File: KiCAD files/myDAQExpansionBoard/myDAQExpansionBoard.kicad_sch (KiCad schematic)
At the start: 71 parts, among them J1 Conn_01x05_Male, J2 Conn_01x05_Male, J3 Conn_01x08_Male, J4 OSTV7XX3151, J5 Screw_Terminal_01x02, J6 Screw_Terminal_01x02, J7 Screw_Terminal_01x01, J8 Screw_Terminal_01x01, SW1 SW_SPDT, SW2 SW_SPDT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

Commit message: update
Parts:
- R1, R20: value 1k -> 4k7
- R10, R11, R13, R14, R15, R16, R8: value 680 -> 4k7
- R5: value 1k -> 2k
- R7: value 1k -> 619
- R9: value 1k -> 6k8
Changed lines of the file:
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@@
     (in_bom yes) (on_board yes)
     (property "Reference" "R7" (id 0) (at 177.419 45.974 90))
-    (property "Value" "1k" (id 1) (at 177.419 48.514 90))
+    (property "Value" "619" (id 1) (at 177.419 48.514 90))
     (property "Footprint" "Resistor_SMD:R_0603_1608Metric" (id 2) (at 177.419 50.292 90)
       (effects (font (size 1.27 1.27)) hide)
@@
     (in_bom yes) (on_board yes)
     (property "Reference" "R9" (id 0) (at 177.419 58.674 90))
-    (property "Value" "1k" (id 1) (at 177.419 61.214 90))
+    (property "Value" "6k8" (id 1) (at 177.419 61.214 90))
     (property "Footprint" "Resistor_SMD:R_0603_1608Metric" (id 2) (at 177.419 62.992 90)
       (effects (font (size 1.27 1.27)) hide)
@@
     (in_bom yes) (on_board yes)
     (property "Reference" "R8" (id 0) (at 166.751 70.104 90))
-    (property "Value" "680" (id 1) (at 166.751 72.009 90))
+    (property "Value" "4k7" (id 1) (at 166.751 72.009 90))
     (property "Footprint" "Resistor_SMD:R_0603_1608Metric" (id 2) (at 166.751 73.787 90)
       (effects (font (size 1.27 1.27)) hide)
@@
     (in_bom yes) (on_board yes)
     (property "Reference" "R1" (id 0) (at 177.419 16.764 90))
-    (property "Value" "1k" (id 1) (at 177.419 19.304 90))
+    (property "Value" "4k7" (id 1) (at 177.419 19.304 90))
     (property "Footprint" "Resistor_SMD:R_0603_1608Metric" (id 2) (at 177.419 21.082 90)
       (effects (font (size 1.27 1.27)) hide)
@@
     (in_bom yes) (on_board yes)
     (property "Reference" "R10" (id 0) (at 166.751 74.549 90))
-    (property "Value" "680" (id 1) (at 166.751 76.454 90))
+    (property "Value" "4k7" (id 1) (at 166.751 76.454 90))
     (property "Footprint" "Resistor_SMD:R_0603_1608Metric" (id 2) (at 166.751 78.232 90)
       (effects (font (size 1.27 1.27)) hide)
@@
     (in_bom yes) (on_board yes)
     (property "Reference" "R11" (id 0) (at 166.751 78.994 90))
-    (property "Value" "680" (id 1) (at 166.751 80.899 90))
+    (property "Value" "4k7" (id 1) (at 166.751 80.899 90))
     (property "Footprint" "Resistor_SMD:R_0603_1608Metric" (id 2) (at 166.751 82.677 90)
       (effects (font (size 1.27 1.27)) hide)
@@
     (in_bom yes) (on_board yes)
     (property "Reference" "R16" (id 0) (at 166.751 96.774 90))
-    (property "Value" "680" (id 1) (at 166.751 98.679 90))
+    (property "Value" "4k7" (id 1) (at 166.751 98.679 90))
     (property "Footprint" "Resistor_SMD:R_0603_1608Metric" (id 2) (at 166.751 100.457 90)
       (effects (font (size 1.27 1.27)) hide)
@@
     (in_bom yes) (on_board yes)
     (property "Reference" "R13" (id 0) (at 166.751 83.439 90))
-    (property "Value" "680" (id 1) (at 166.751 85.344 90))
+    (property "Value" "4k7" (id 1) (at 166.751 85.344 90))
     (property "Footprint" "Resistor_SMD:R_0603_1608Metric" (id 2) (at 166.751 87.122 90)
       (effects (font (size 1.27 1.27)) hide)
@@
     (in_bom yes) (on_board yes)
     (property "Reference" "R5" (id 0) (at 177.419 32.639 90))
-    (property "Value" "1k" (id 1) (at 177.419 35.179 90))
+    (property "Value" "2k" (id 1) (at 177.419 35.179 90))
     (property "Footprint" "Resistor_SMD:R_0603_1608Metric" (id 2) (at 177.419 36.957 90)
       (effects (font (size 1.27 1.27)) hide)
@@
     (in_bom yes) (on_board yes)
     (property "Reference" "R20" (id 0) (at 216.535 90.297 0))
-    (property "Value" "1k" (id 1) (at 219.71 90.297 90))
+    (property "Value" "4k7" (id 1) (at 219.71 90.297 90))
     (property "Footprint" "Resistor_SMD:R_0603_1608Metric" (id 2) (at 217.932 90.297 90)
       (effects (font (size 1.27 1.27)) hide)
@@
     (in_bom yes) (on_board yes)
     (property "Reference" "R15" (id 0) (at 166.751 92.329 90))
-    (property "Value" "680" (id 1) (at 166.751 94.234 90))
+    (property "Value" "4k7" (id 1) (at 166.751 94.234 90))
     (property "Footprint" "Resistor_SMD:R_0603_1608Metric" (id 2) (at 166.751 96.012 90)
       (effects (font (size 1.27 1.27)) hide)
@@
     (in_bom yes) (on_board yes)
     (property "Reference" "R14" (id 0) (at 166.751 87.884 90))
-    (property "Value" "680" (id 1) (at 166.751 89.789 90))
+    (property "Value" "4k7" (id 1) (at 166.751 89.789 90))
     (property "Footprint" "Resistor_SMD:R_0603_1608Metric" (id 2) (at 166.751 91.567 90)
       (effects (font (size 1.27 1.27)) hide)
@@
     )
     (path "/433b0c6c-361b-44cd-99c3-351dd671e9c9"
-      (reference "R1") (unit 1) (value "1k") (footprint "Resistor_SMD:R_0603_1608Metric")
+      (reference "R1") (unit 1) (value "4k7") (footprint "Resistor_SMD:R_0603_1608Metric")
     )
     (path "/f78db9fb-cb90-4b5a-a4c3-fa1ddcd96b2f"
@@
     )
     (path "/bc772a1b-5451-41db-9c2f-d7edb0c376e2"
-      (reference "R5") (unit 1) (value "1k") (footprint "Resistor_SMD:R_0603_1608Metric")
+      (reference "R5") (unit 1) (value "2k") (footprint "Resistor_SMD:R_0603_1608Metric")
     )
     (path "/ca6ccc26-d3b9-4b88-bfa0-85358f769c5a"
@@
     )
     (path "/085dede5-e78e-4e86-8f9f-0e5465cc00b9"
-      (reference "R7") (unit 1) (value "1k") (footprint "Resistor_SMD:R_0603_1608Metric")
+      (reference "R7") (unit 1) (value "619") (footprint "Resistor_SMD:R_0603_1608Metric")
     )
     (path "/2ba9d9c0-5d0a-4be1-afe4-2de9cfa25c42"
-      (reference "R8") (unit 1) (value "680") (footprint "Resistor_SMD:R_0603_1608Metric")
+      (reference "R8") (unit 1) (value "4k7") (footprint "Resistor_SMD:R_0603_1608Metric")
     )
     (path "/15ef9b16-b6d9-46b2-bd55-e3bd55127ab3"
-      (reference "R9") (unit 1) (value "1k") (footprint "Resistor_SMD:R_0603_1608Metric")
+      (reference "R9") (unit 1) (value "6k8") (footprint "Resistor_SMD:R_0603_1608Metric")
     )
     (path "/525c708d-edd2-4368-bbec-bf4b6e9c0ace"
-      (reference "R10") (unit 1) (value "680") (footprint "Resistor_SMD:R_0603_1608Metric")
+      (reference "R10") (unit 1) (value "4k7") (footprint "Resistor_SMD:R_0603_1608Metric")
     )
     (path "/7212c595-395e-40b8-bda9-f190b9683d3b"
-      (reference "R11") (unit 1) (value "680") (footprint "Resistor_SMD:R_0603_1608Metric")
+      (reference "R11") (unit 1) (value "4k7") (footprint "Resistor_SMD:R_0603_1608Metric")
     )
     (path "/b4dfd47d-e445-4115-b914-f93c8ca70c01"
@@
     )
     (path "/b4ebc770-9ee9-4695-b41e-2c705582fd44"
-      (reference "R13") (unit 1) (value "680") (footprint "Resistor_SMD:R_0603_1608Metric")
+      (reference "R13") (unit 1) (value "4k7") (footprint "Resistor_SMD:R_0603_1608Metric")
     )
     (path "/fd4b6262-dad5-45ce-9480-0b0623b0e919"
-      (reference "R14") (unit 1) (value "680") (footprint "Resistor_SMD:R_0603_1608Metric")
+      (reference "R14") (unit 1) (value "4k7") (footprint "Resistor_SMD:R_0603_1608Metric")
     )
     (path "/ed2f2cb4-07ba-406b-bf66-2ddd22ebe99b"
-      (reference "R15") (unit 1) (value "680") (footprint "Resistor_SMD:R_0603_1608Metric")
+      (reference "R15") (unit 1) (value "4k7") (footprint "Resistor_SMD:R_0603_1608Metric")
     )
     (path "/ab9b29b0-c429-48b0-9aad-ff945e1e65b3"
-      (reference "R16") (unit 1) (value "680") (footprint "Resistor_SMD:R_0603_1608Metric")
+      (reference "R16") (unit 1) (value "4k7") (footprint "Resistor_SMD:R_0603_1608Metric")
     )
     (path "/97abf834-da84-49dd-ace7-84d78a8c1b0f"
@@
     )
     (path "/d27373d0-8f97-432f-9664-fb2c66cf74ea"
-      (reference "R20") (unit 1) (value "1k") (footprint "Resistor_SMD:R_0603_1608Metric")
+      (reference "R20") (unit 1) (value "4k7") (footprint "Resistor_SMD:R_0603_1608Metric")
     )
     (path "/951d8e55-0983-48e1-a0c4-bac48479355a"

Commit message: update
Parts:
- R10, R11, R13, R14, R15, R16, R8: value 4k7 -> 2k
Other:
- note added: "*2k otpronici za crveni 7segm display (4.6V VCC)"
- note removed: "SN74LS74 (6kn u electronic centru)"
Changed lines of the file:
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@@
     (effects (font (size 2 2)) (justify left bottom))
   )
-  (text "SN74LS74 (6kn u electronic centru)" (at 97.282 104.14 0)
+  (text "*2k otpronici za crveni 7segm display (4.6V VCC)" (at 97.282 104.14 0)
     (effects (font (size 1.27 1.27)) (justify left bottom))
   )
@@
     (in_bom yes) (on_board yes)
     (property "Reference" "R8" (id 0) (at 166.751 70.104 90))
-    (property "Value" "4k7" (id 1) (at 166.751 72.009 90))
+    (property "Value" "2k" (id 1) (at 166.751 72.009 90))
     (property "Footprint" "Resistor_SMD:R_0603_1608Metric" (id 2) (at 166.751 73.787 90)
       (effects (font (size 1.27 1.27)) hide)
@@
     (in_bom yes) (on_board yes)
     (property "Reference" "R10" (id 0) (at 166.751 74.549 90))
-    (property "Value" "4k7" (id 1) (at 166.751 76.454 90))
+    (property "Value" "2k" (id 1) (at 166.751 76.454 90))
     (property "Footprint" "Resistor_SMD:R_0603_1608Metric" (id 2) (at 166.751 78.232 90)
       (effects (font (size 1.27 1.27)) hide)
@@
     (in_bom yes) (on_board yes)
     (property "Reference" "R11" (id 0) (at 166.751 78.994 90))
-    (property "Value" "4k7" (id 1) (at 166.751 80.899 90))
+    (property "Value" "2k" (id 1) (at 166.751 80.899 90))
     (property "Footprint" "Resistor_SMD:R_0603_1608Metric" (id 2) (at 166.751 82.677 90)
       (effects (font (size 1.27 1.27)) hide)
@@
     (in_bom yes) (on_board yes)
     (property "Reference" "R16" (id 0) (at 166.751 96.774 90))
-    (property "Value" "4k7" (id 1) (at 166.751 98.679 90))
+    (property "Value" "2k" (id 1) (at 166.751 98.679 90))
     (property "Footprint" "Resistor_SMD:R_0603_1608Metric" (id 2) (at 166.751 100.457 90)
       (effects (font (size 1.27 1.27)) hide)
@@
     (in_bom yes) (on_board yes)
     (property "Reference" "R13" (id 0) (at 166.751 83.439 90))
-    (property "Value" "4k7" (id 1) (at 166.751 85.344 90))
+    (property "Value" "2k" (id 1) (at 166.751 85.344 90))
     (property "Footprint" "Resistor_SMD:R_0603_1608Metric" (id 2) (at 166.751 87.122 90)
       (effects (font (size 1.27 1.27)) hide)
@@
     (in_bom yes) (on_board yes)
     (property "Reference" "R15" (id 0) (at 166.751 92.329 90))
-    (property "Value" "4k7" (id 1) (at 166.751 94.234 90))
+    (property "Value" "2k" (id 1) (at 166.751 94.234 90))
     (property "Footprint" "Resistor_SMD:R_0603_1608Metric" (id 2) (at 166.751 96.012 90)
       (effects (font (size 1.27 1.27)) hide)
@@
     (in_bom yes) (on_board yes)
     (property "Reference" "R14" (id 0) (at 166.751 87.884 90))
-    (property "Value" "4k7" (id 1) (at 166.751 89.789 90))
+    (property "Value" "2k" (id 1) (at 166.751 89.789 90))
     (property "Footprint" "Resistor_SMD:R_0603_1608Metric" (id 2) (at 166.751 91.567 90)
       (effects (font (size 1.27 1.27)) hide)
@@
     )
     (path "/2ba9d9c0-5d0a-4be1-afe4-2de9cfa25c42"
-      (reference "R8") (unit 1) (value "4k7") (footprint "Resistor_SMD:R_0603_1608Metric")
+      (reference "R8") (unit 1) (value "2k") (footprint "Resistor_SMD:R_0603_1608Metric")
     )
     (path "/15ef9b16-b6d9-46b2-bd55-e3bd55127ab3"
@@
     )
     (path "/525c708d-edd2-4368-bbec-bf4b6e9c0ace"
-      (reference "R10") (unit 1) (value "4k7") (footprint "Resistor_SMD:R_0603_1608Metric")
+      (reference "R10") (unit 1) (value "2k") (footprint "Resistor_SMD:R_0603_1608Metric")
     )
     (path "/7212c595-395e-40b8-bda9-f190b9683d3b"
-      (reference "R11") (unit 1) (value "4k7") (footprint "Resistor_SMD:R_0603_1608Metric")
+      (reference "R11") (unit 1) (value "2k") (footprint "Resistor_SMD:R_0603_1608Metric")
     )
     (path "/b4dfd47d-e445-4115-b914-f93c8ca70c01"
@@
     )
     (path "/b4ebc770-9ee9-4695-b41e-2c705582fd44"
-      (reference "R13") (unit 1) (value "4k7") (footprint "Resistor_SMD:R_0603_1608Metric")
+      (reference "R13") (unit 1) (value "2k") (footprint "Resistor_SMD:R_0603_1608Metric")
     )
     (path "/fd4b6262-dad5-45ce-9480-0b0623b0e919"
-      (reference "R14") (unit 1) (value "4k7") (footprint "Resistor_SMD:R_0603_1608Metric")
+      (reference "R14") (unit 1) (value "2k") (footprint "Resistor_SMD:R_0603_1608Metric")
     )
     (path "/ed2f2cb4-07ba-406b-bf66-2ddd22ebe99b"
-      (reference "R15") (unit 1) (value "4k7") (footprint "Resistor_SMD:R_0603_1608Metric")
+      (reference "R15") (unit 1) (value "2k") (footprint "Resistor_SMD:R_0603_1608Metric")
     )
     (path "/ab9b29b0-c429-48b0-9aad-ff945e1e65b3"
-      (reference "R16") (unit 1) (value "4k7") (footprint "Resistor_SMD:R_0603_1608Metric")
+      (reference "R16") (unit 1) (value "2k") (footprint "Resistor_SMD:R_0603_1608Metric")
     )
     (path "/97abf834-da84-49dd-ace7-84d78a8c1b0f"

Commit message: Update myDAQExpansionBoard.kicad_sch
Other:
- note added: "*2k otpronici za crveni 7segm display"
- note added: "7SEGM + IC SN74LS47"
- note removed: "*2k otpronici za crveni 7segm display (4.6V VCC)"
- note removed: "7SEGM + IC SN74LS74"
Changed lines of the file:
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@@
     (effects (font (size 2 2)) (justify left bottom))
   )
-  (text "*2k otpronici za crveni 7segm display (4.6V VCC)" (at 97.282 104.14 0)
+  (text "*2k otpronici za crveni 7segm display" (at 90.17 108.585 0)
     (effects (font (size 1.27 1.27)) (justify left bottom))
   )
@@
     (effects (font (size 2 2)) (justify left bottom))
   )
-  (text "7SEGM + IC SN74LS74" (at 96.901 70.739 0)
+  (text "7SEGM + IC SN74LS47" (at 96.901 70.739 0)
     (effects (font (size 2 2)) (justify left bottom))
   )

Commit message: BOMv1
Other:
- note added: "BILJEŠKE: - BOM se nalazi u bom folderu, datoteka se zove myDAQExpansionBoard.xlsx"
- note removed: "MONTAŽA: - jumperi moraju biti oni koji imaju ručicu"
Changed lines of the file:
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@@
     (effects (font (size 2 2)) (justify left bottom))
   )
-  (text "MONTAŽA:\n- jumperi moraju biti oni koji imaju ručicu"
-    (at 15.24 161.29 0)
-    (effects (font (size 1.27 1.27)) (justify left bottom))
+  (text "BILJEŠKE:\n\n- BOM se nalazi u bom folderu, datoteka se zove myDAQExpansionBoard.xlsx"
+    (at 15.24 185.42 0)
+    (effects (font (size 2.54 2.54)) (justify left bottom))
   )
   (text "MON. RUPE" (at 14.986 88.9 0)

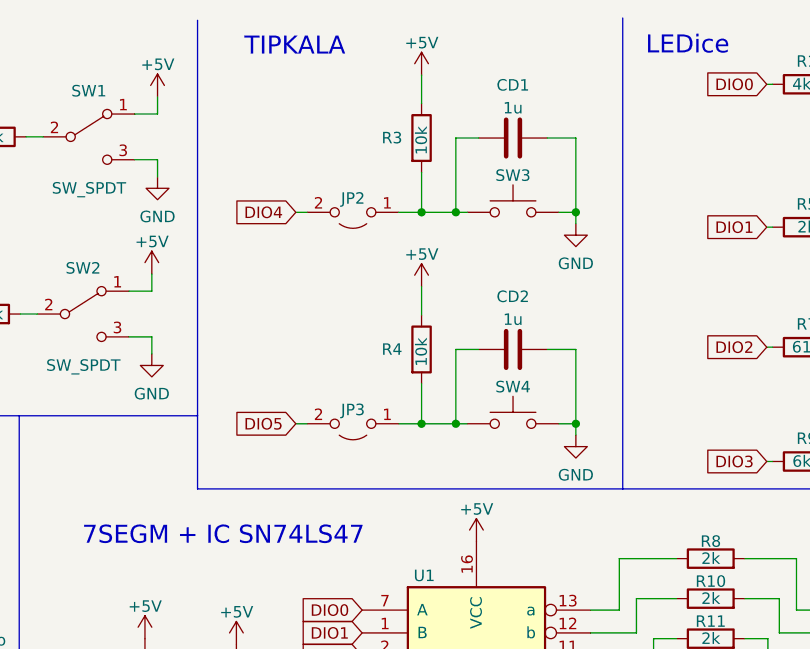
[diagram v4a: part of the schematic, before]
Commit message: Added resistor for RC circuit
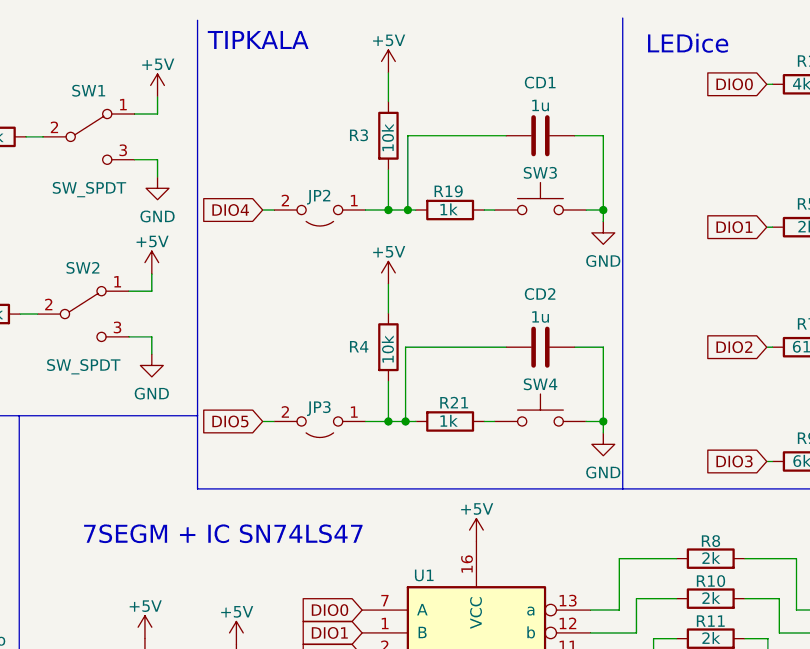
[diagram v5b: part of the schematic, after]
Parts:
- added R19, R21: 1k, Resistor_SMD:R_0603_1608Metric, symbol Device:R
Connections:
- net at CD1.1, JP2.1 (A), R3.2: now also R19.2; no longer SW3.1
- net at CD2.1, JP3.1 (A), R4.2: now also R21.2; no longer SW4.1
- new net: R21.1, SW4.1
- new net: R19.1, SW3.1
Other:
- moved on the sheet: CD1, CD2, JP2, JP3, R3, R4, SW3, SW4

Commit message: update
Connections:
- net DIO0: now also JP2.2 (B); no longer R1.1, U1.7 (A), U4.5 (IN1)
- net DIO1: now also R1.1, U1.7 (A); no longer R5.1, U1.1 (B)
- net DIO2: now also JP3.2 (B); no longer R7.1, U1.2 (C), U4.10 (IN3)
- net DIO3: now also R5.1, U1.1 (B), U4.5 (IN1); no longer R9.1, U1.6 (D), U4.12 (IN4)
- net DIO4: now also JP4.2 (B); no longer JP2.2 (B)
- net DIO5: now also R7.1, U1.2 (C), U4.10 (IN3); no longer JP3.2 (B)
- net DIO7: now also R9.1, U1.6 (D), U4.12 (IN4); no longer JP4.2 (B)

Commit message: v1rev2
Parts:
- SW1, SW2: footprint Library:we01014042 -> Library:500SSP1S1M2QEA
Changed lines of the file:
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@@
     (property "Reference" "SW1" (id 0) (at 97.663 20.066 0))
     (property "Value" "SW_SPDT" (id 1) (at 97.663 30.861 0))
-    (property "Footprint" "Library:we01014042" (id 2) (at 97.663 25.146 0)
+    (property "Footprint" "Library:500SSP1S1M2QEA" (id 2) (at 97.663 25.146 0)
       (effects (font (size 1.27 1.27)) hide)
     )
@@
     (property "Reference" "SW2" (id 0) (at 97.028 39.751 0))
     (property "Value" "SW_SPDT" (id 1) (at 97.028 50.546 0))
-    (property "Footprint" "Library:we01014042" (id 2) (at 97.028 44.831 0)
+    (property "Footprint" "Library:500SSP1S1M2QEA" (id 2) (at 97.028 44.831 0)
       (effects (font (size 1.27 1.27)) hide)
     )
@@
     )
     (path "/7078f9f8-f76c-4524-96a7-1f5a2c6a03e5"
-      (reference "SW1") (unit 1) (value "SW_SPDT") (footprint "Library:we01014042")
+      (reference "SW1") (unit 1) (value "SW_SPDT") (footprint "Library:500SSP1S1M2QEA")
     )
     (path "/bb50f314-d057-4b1a-9b4d-ff176329b7ae"
-      (reference "SW2") (unit 1) (value "SW_SPDT") (footprint "Library:we01014042")
+      (reference "SW2") (unit 1) (value "SW_SPDT") (footprint "Library:500SSP1S1M2QEA")
     )
     (path "/90f2d58e-a255-450d-bc74-dbc1a747cc3e"

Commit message: update
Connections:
- net DIO0: now also JP1.2 (B); no longer JP2.2 (B)
- net DIO2: now also JP4.2 (B); no longer JP3.2 (B)
- net DIO4: now also JP3.2 (B); no longer JP4.2 (B)
- net DIO6: now also JP2.2 (B); no longer JP1.2 (B)
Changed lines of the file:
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@@
     )
   )
-  (global_label "DIO4" (shape input) (at 67.818 44.831 180) (fields_autoplaced)
+  (global_label "DIO4" (shape input) (at 116.967 56.769 180) (fields_autoplaced)
     (effects (font (size 1.27 1.27)) (justify right))
-    (property "Intersheet References" "${INTERSHEET_REFS}" (id 0) (at 60.9901 44.7516 0)
+    (property "Intersheet References" "${INTERSHEET_REFS}" (id 0) (at 110.1391 56.6896 0)
       (effects (font (size 1.27 1.27)) (justify right) hide)
     )
@@
     )
   )
-  (global_label "DIO2" (shape input) (at 116.967 56.769 180) (fields_autoplaced)
+  (global_label "DIO2" (shape input) (at 67.818 44.831 180) (fields_autoplaced)
     (effects (font (size 1.27 1.27)) (justify right))
-    (property "Intersheet References" "${INTERSHEET_REFS}" (id 0) (at 110.1391 56.6896 0)
+    (property "Intersheet References" "${INTERSHEET_REFS}" (id 0) (at 60.9901 44.7516 0)
       (effects (font (size 1.27 1.27)) (justify right) hide)
     )
@@
     )
   )
-  (global_label "DIO6" (shape input) (at 68.453 25.146 180) (fields_autoplaced)
+  (global_label "DIO6" (shape input) (at 116.967 33.274 180) (fields_autoplaced)
     (effects (font (size 1.27 1.27)) (justify right))
-    (property "Intersheet References" "${INTERSHEET_REFS}" (id 0) (at 61.6251 25.0666 0)
+    (property "Intersheet References" "${INTERSHEET_REFS}" (id 0) (at 110.1391 33.1946 0)
       (effects (font (size 1.27 1.27)) (justify right) hide)
     )
@@
     )
   )
-  (global_label "DIO0" (shape input) (at 116.967 33.274 180) (fields_autoplaced)
+  (global_label "DIO0" (shape input) (at 68.453 25.146 180) (fields_autoplaced)
     (effects (font (size 1.27 1.27)) (justify right))
-    (property "Intersheet References" "${INTERSHEET_REFS}" (id 0) (at 110.1391 33.3534 0)
+    (property "Intersheet References" "${INTERSHEET_REFS}" (id 0) (at 61.6251 25.2254 0)
       (effects (font (size 1.27 1.27)) (justify right) hide)
     )
